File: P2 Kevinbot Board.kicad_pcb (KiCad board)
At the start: 2 copper layers, 196.5 x 95.4 mm, 72 parts, among them J1 Screw_Terminal_01x02, J10 Conn_01x04, J11 Conn_01x04_Male, J12 Conn_02x06_Odd_Even, J13 Conn_01x04, J14 Conn_01x02, J15 Conn_01x04, J16 Conn_02x06_Odd_Even, J17 Conn_04x03_Servo, J18 Conn_04x03_Servo, J19 Conn_04x03_Servo, J2 Conn_01x03_Male, J20 Conn_04x03_Servo, J21 Conn_01x02, J22 Conn_01x05, J23 Conn_01x05, J24 Conn_01x05, J25 Conn_01x05, J26 Conn_04x03_Servo, J27 Conn_04x03_Servo, J28 Conn_04x03_Servo, J29 Conn_04x03_Servo, J3 Screw_Terminal_01x02, J30 Conn_01x02_Pin, J31 Conn_01x02, J4 Screw_Terminal_01x02, J5 Screw_Terminal_01x02, J6 Conn_02x06_Odd_Even, J7 Conn_01x04, J8 Conn_02x06_Odd_Even, J9 Screw_Terminal_01x02, Q1 IRLML6402, SW1 SW_Push, U1 P2_EDGE_MODULE_SOCKET, U2 DS18B20, U3 PCA9685PW, U4 TC4427, U5 PCA9685PW

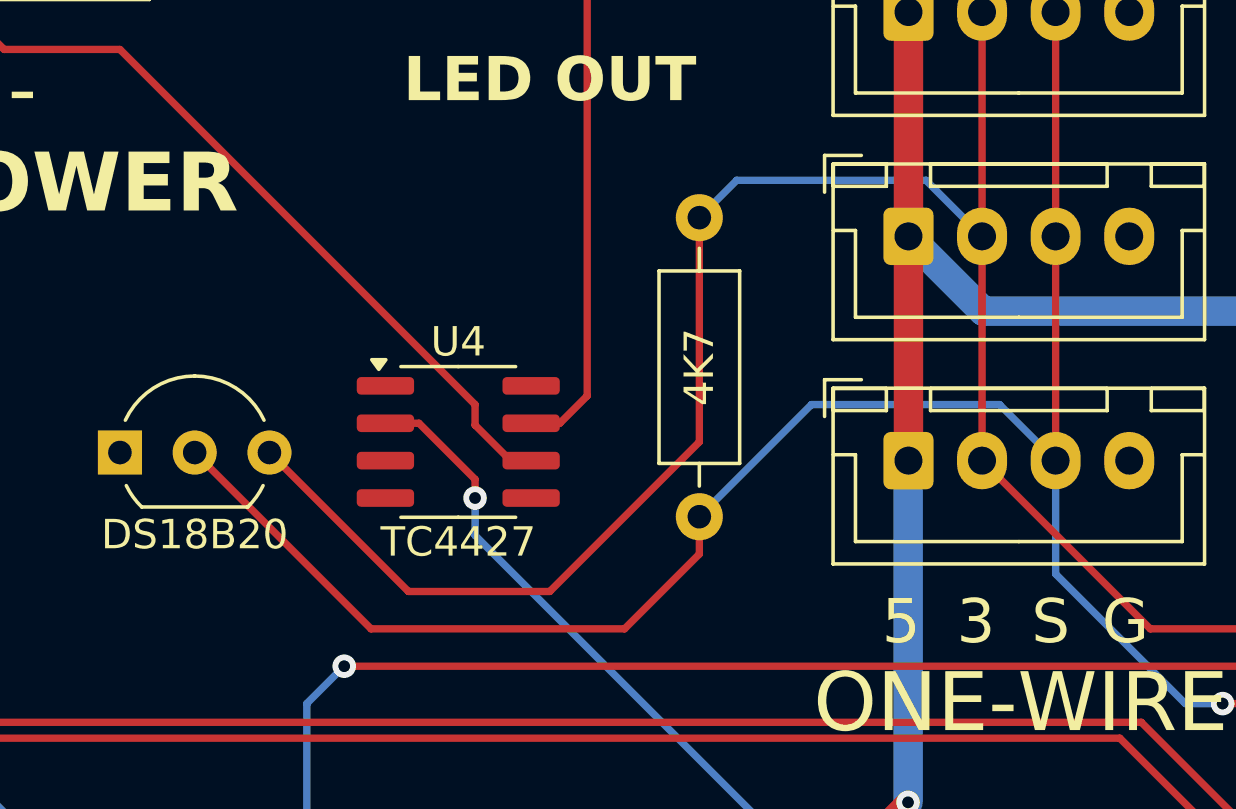
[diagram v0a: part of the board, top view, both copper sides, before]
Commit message: Change logo, led resistors
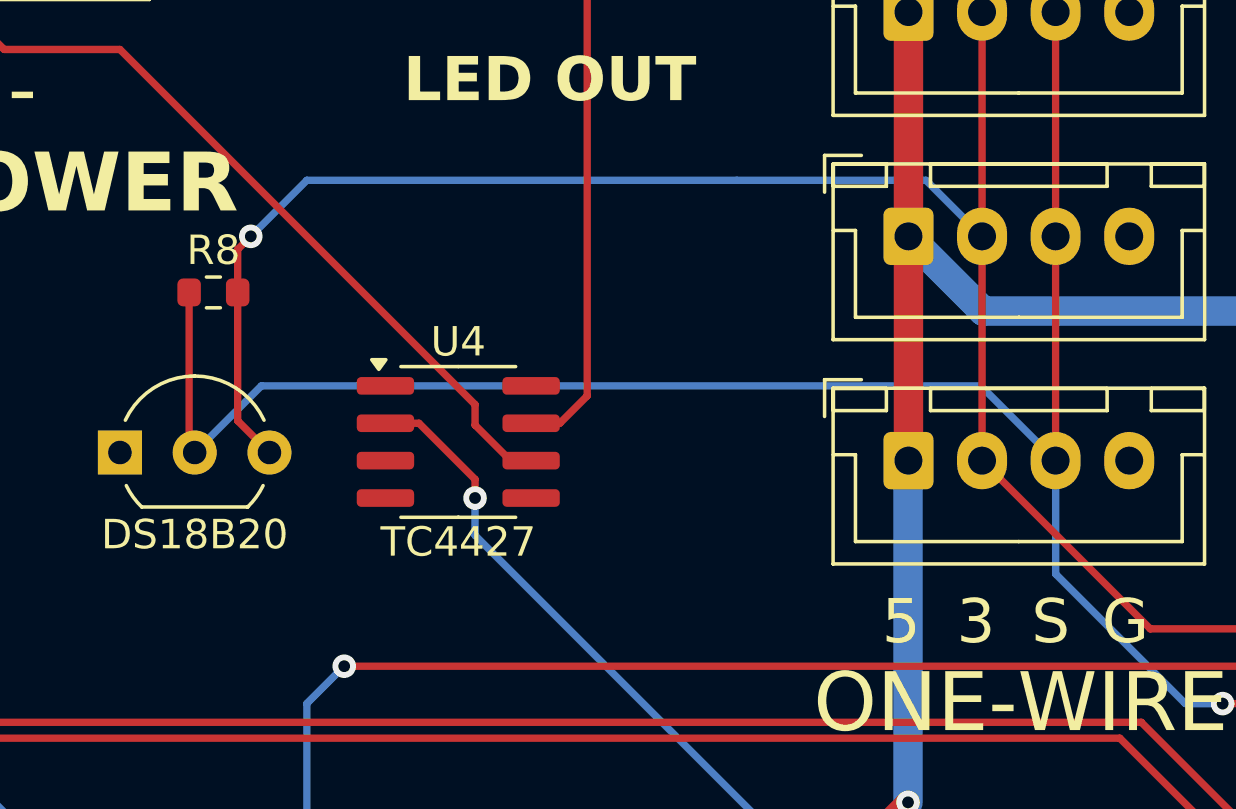
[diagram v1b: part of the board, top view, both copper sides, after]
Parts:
- R1: value 360R -> 620R
- R2: value 180R -> 270R
- R3: value 180R -> 820R
- R8: footprint Resistor_THT:R_Axial_DIN0207_L6.3mm_D2.5mm_P10.16mm_Horizontal -> Resistor_SMD:R_0603_1608Metric
- moved R8 18.2 mm to (114.4, 77.5), turned to 0 degrees
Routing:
- net P2_V32: track 123.7 -> 120.9 mm, vias 0 -> 1

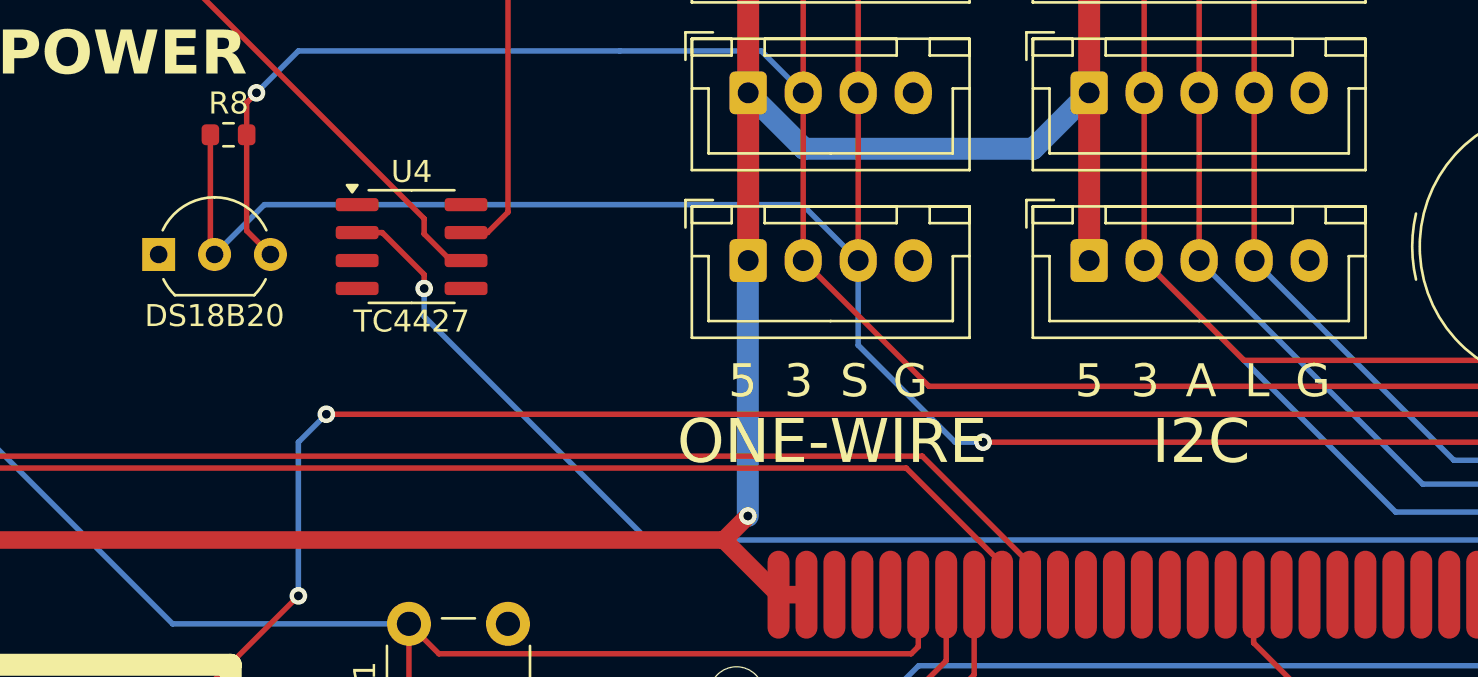
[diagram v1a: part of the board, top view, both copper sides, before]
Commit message: DRC fixes, add missing library, misc
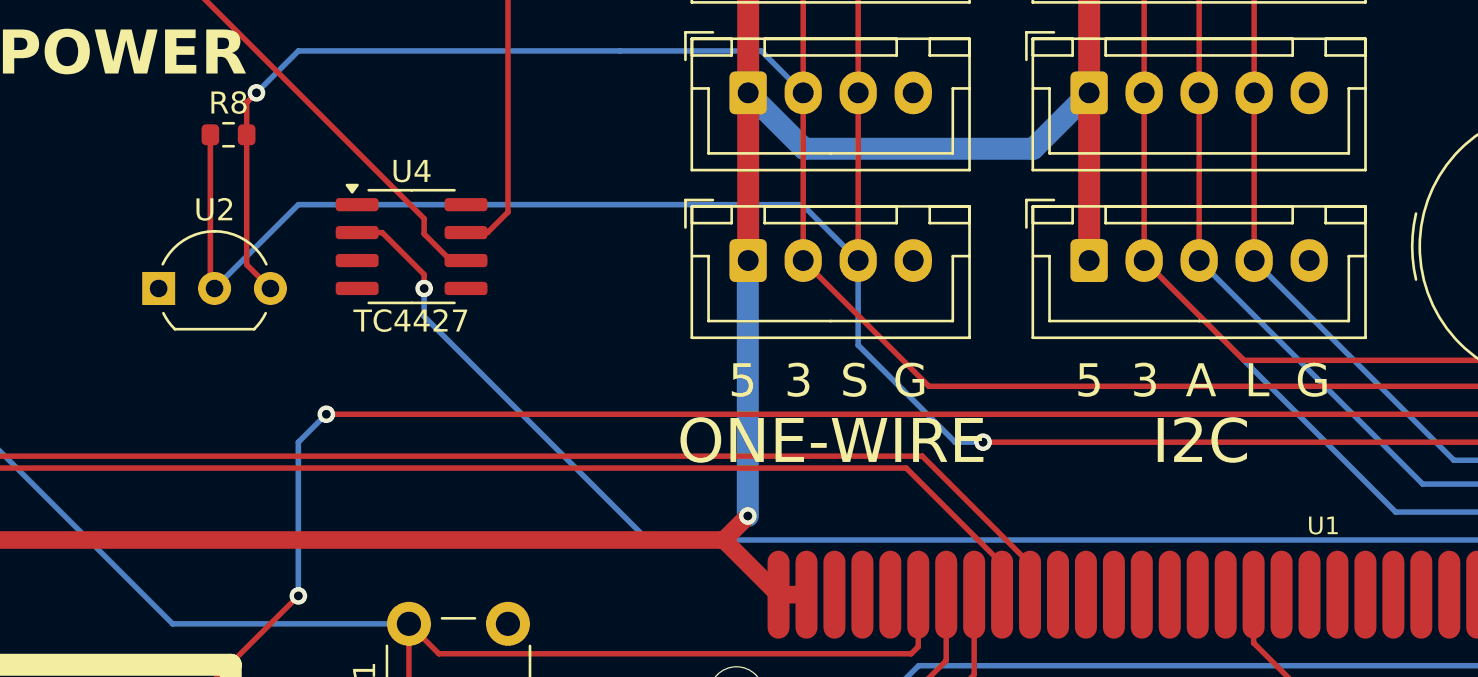
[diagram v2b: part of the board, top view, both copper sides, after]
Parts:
- moved U2 1.54 mm to (111.3, 84.5)
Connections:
- net -BATT renamed GND
- U1 pad 59: P2_P55 -> unconnected-(U1-P55-Pad59)
- U1 pad 60: P2_P54 -> unconnected-(U1-P54-Pad60)
- U1 pad 61: P2_P53 -> unconnected-(U1-P53-Pad61)
- U1 pad 62: P2_P52 -> unconnected-(U1-P52-Pad62)
- U1 pad 63: P2_P51 -> unconnected-(U1-P51-Pad63)
- U1 pad 64: P2_P50 -> unconnected-(U1-P50-Pad64)
- U1 pad 65: P2_P49 -> unconnected-(U1-P49-Pad65)
- U1 pad 66: P2_P48 -> unconnected-(U1-P48-Pad66)
- U1 pad 67: P2_V48 -> unconnected-(U1-V48-Pad67)
- U1 pad 69: P2_P47 -> unconnected-(U1-P47-Pad69)
- U1 pad 7: P2_P33 -> unconnected-(U1-P33-Pad7)
- U1 pad 70: P2_P46 -> unconnected-(U1-P46-Pad70)
- U1 pad 71: P2_P45 -> unconnected-(U1-P45-Pad71)
- U1 pad 72: P2_P44 -> unconnected-(U1-P44-Pad72)
- U1 pad 73: P2_P43 -> unconnected-(U1-P43-Pad73)
- U1 pad 8: P2_P32 -> unconnected-(U1-P32-Pad8)
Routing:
- net P2_P39: track 113.4 -> 115.6 mm
- net P2_V32: track 120.9 -> 122.4 mm

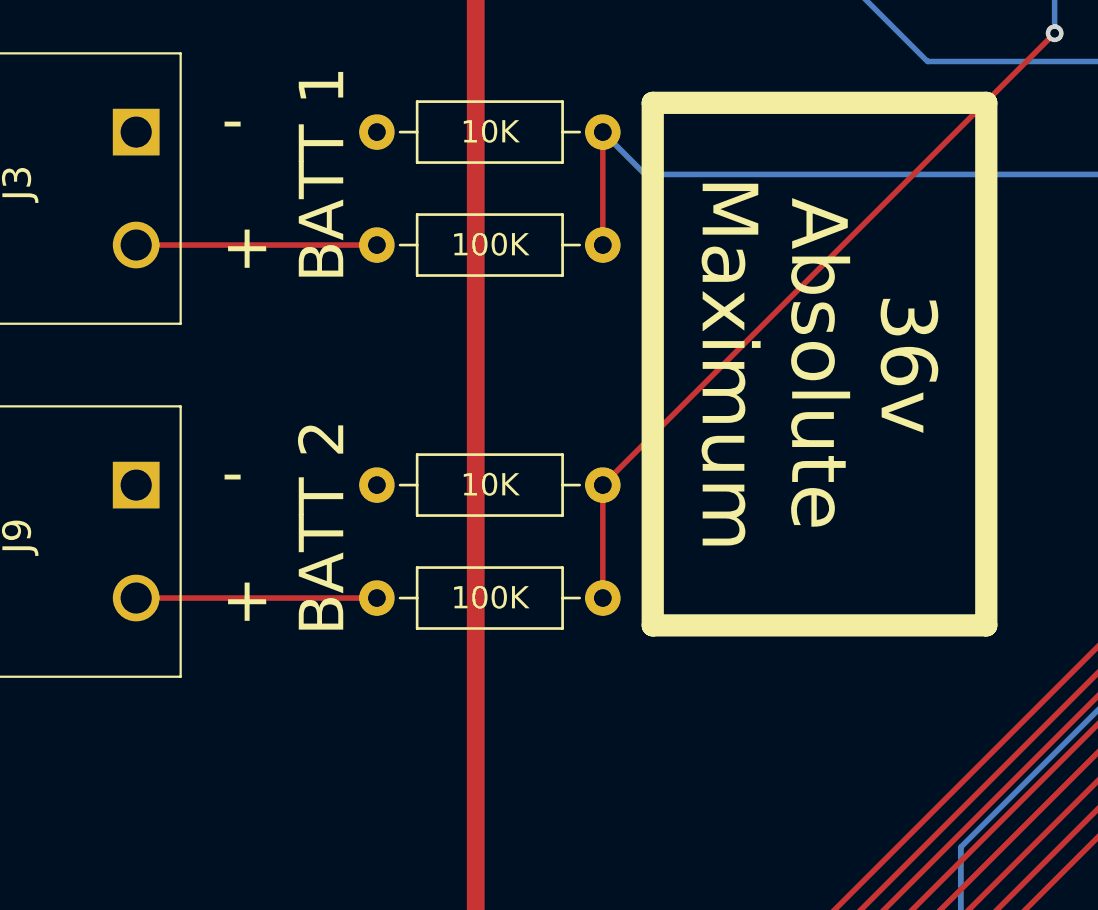
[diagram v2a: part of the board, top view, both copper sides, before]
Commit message: Add voltmeter polyfuses
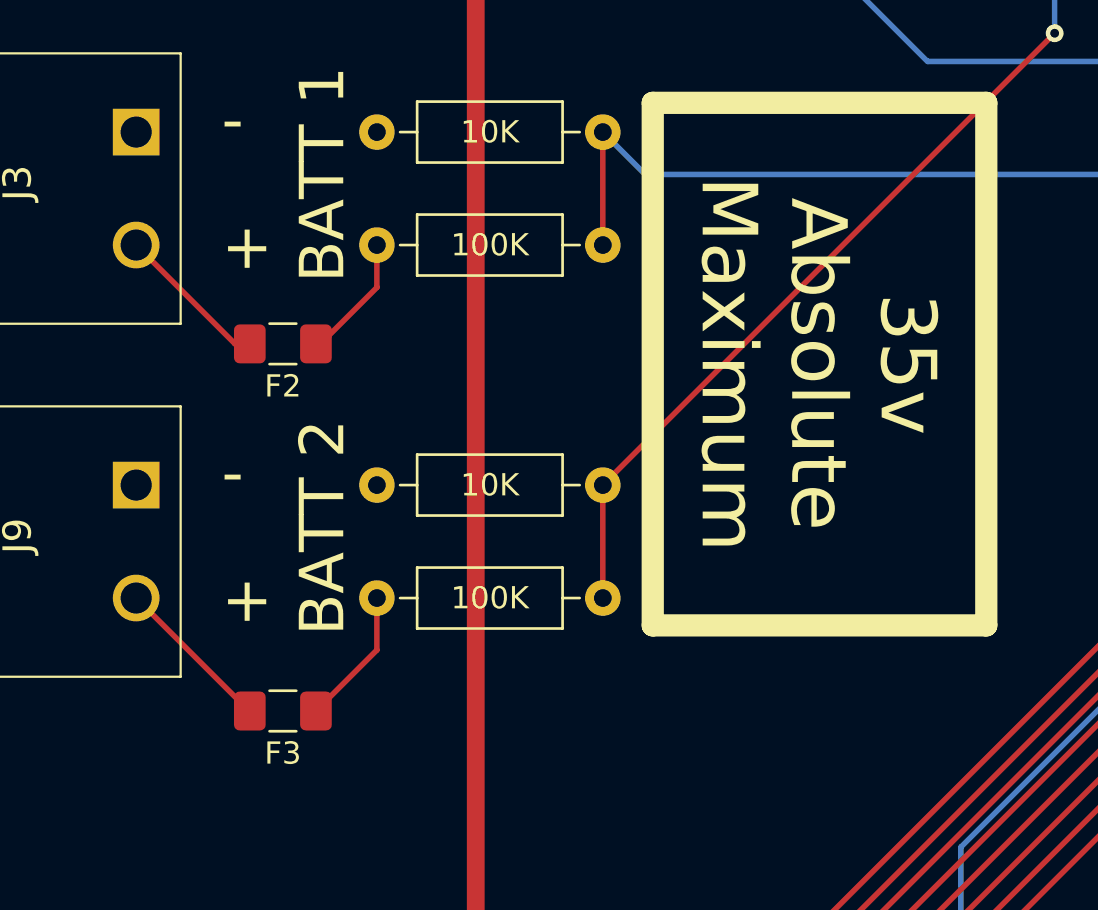
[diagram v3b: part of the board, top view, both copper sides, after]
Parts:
- added F2: Polyfuse_Small, Fuse:Fuse_1206_3216Metric_Pad1.42x1.75mm_HandSolder, F.Cu at (82.9, 112.4)
- added F3: Polyfuse_Small, Fuse:Fuse_1206_3216Metric_Pad1.42x1.75mm_HandSolder, F.Cu at (82.9, 128.9)
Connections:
- R4 pad 2: +BATT -> Net-(F2-Pad2)
- R6 pad 2: Net-(J9-Pin_2) -> Net-(F3-Pad1)
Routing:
- net Net-(F3-Pad1): track 0.00 -> 6.21 mm
- net Net-(F2-Pad2): track 0.00 -> 5.50 mm
- net +BATT: track 10.8 -> 7.15 mm
- net Net-(J9-Pin_2): track 10.8 -> 7.21 mm
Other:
- board text added: "35v Absolute Maximum"
- board text removed: "36v Absolute Maximum"

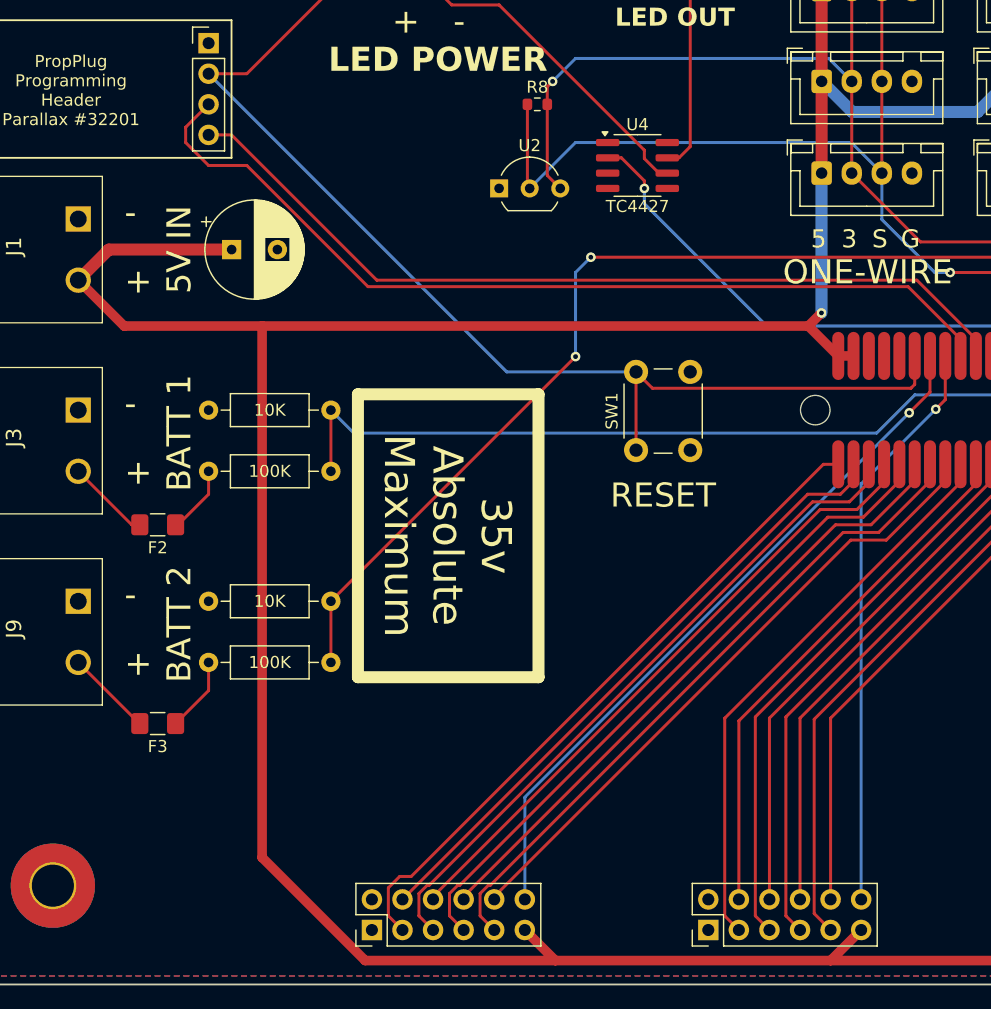
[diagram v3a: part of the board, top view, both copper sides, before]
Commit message: Add main fuse
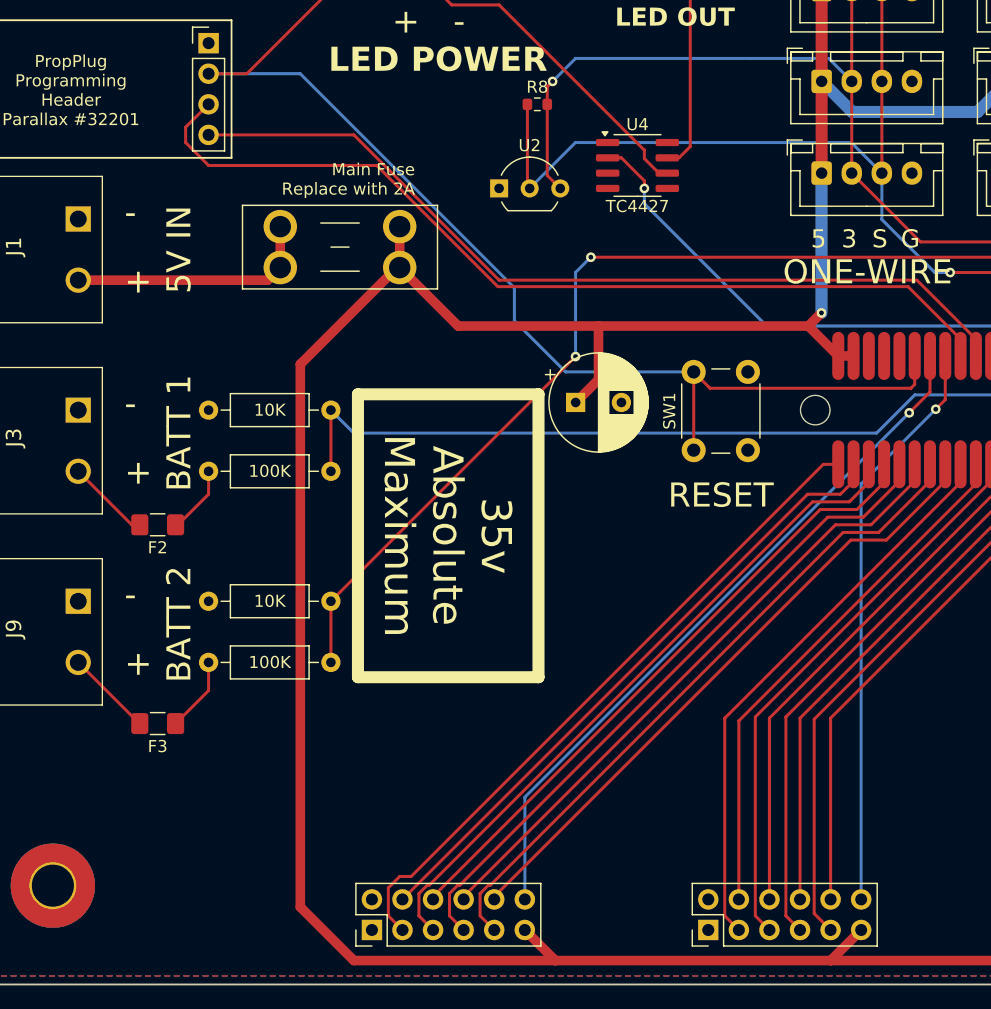
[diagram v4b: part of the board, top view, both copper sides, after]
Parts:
- added F4: Fuse, Fuse:Fuseholder_Blade_Mini_Keystone_3568, F.Cu at (93.1, 87.6)
- moved C1 31.3 mm to (117.6, 102.2)
- moved SW1 4.79 mm to (127.4, 106.2)
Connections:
- J1 pad 2: +5V -> Net-(J1-Pin_2)
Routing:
- net +5V: track 526.2 -> 504.3 mm
- net Net-(J1-Pin_2): track 0.00 -> 20.6 mm
- net P2_RESn: track 187.9 -> 189.5 mm
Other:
- board text added: "Main Fuse Replace with 2A"

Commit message: Logo changes
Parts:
- added G***: LOGO, MoreSymbols:KevinbotV3-New, B.Cu at (164.3, 129.5)
